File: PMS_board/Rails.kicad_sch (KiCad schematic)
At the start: 36 parts, among them J1 D1, J10 CORE, J11 DRIVE, J12 JETSON, J13 AUX1, J14 AUX2, J2 D2, J3 D3, J4 D4, J5 T1, J6 T2, J7 T3, J8 T4, J9 NET

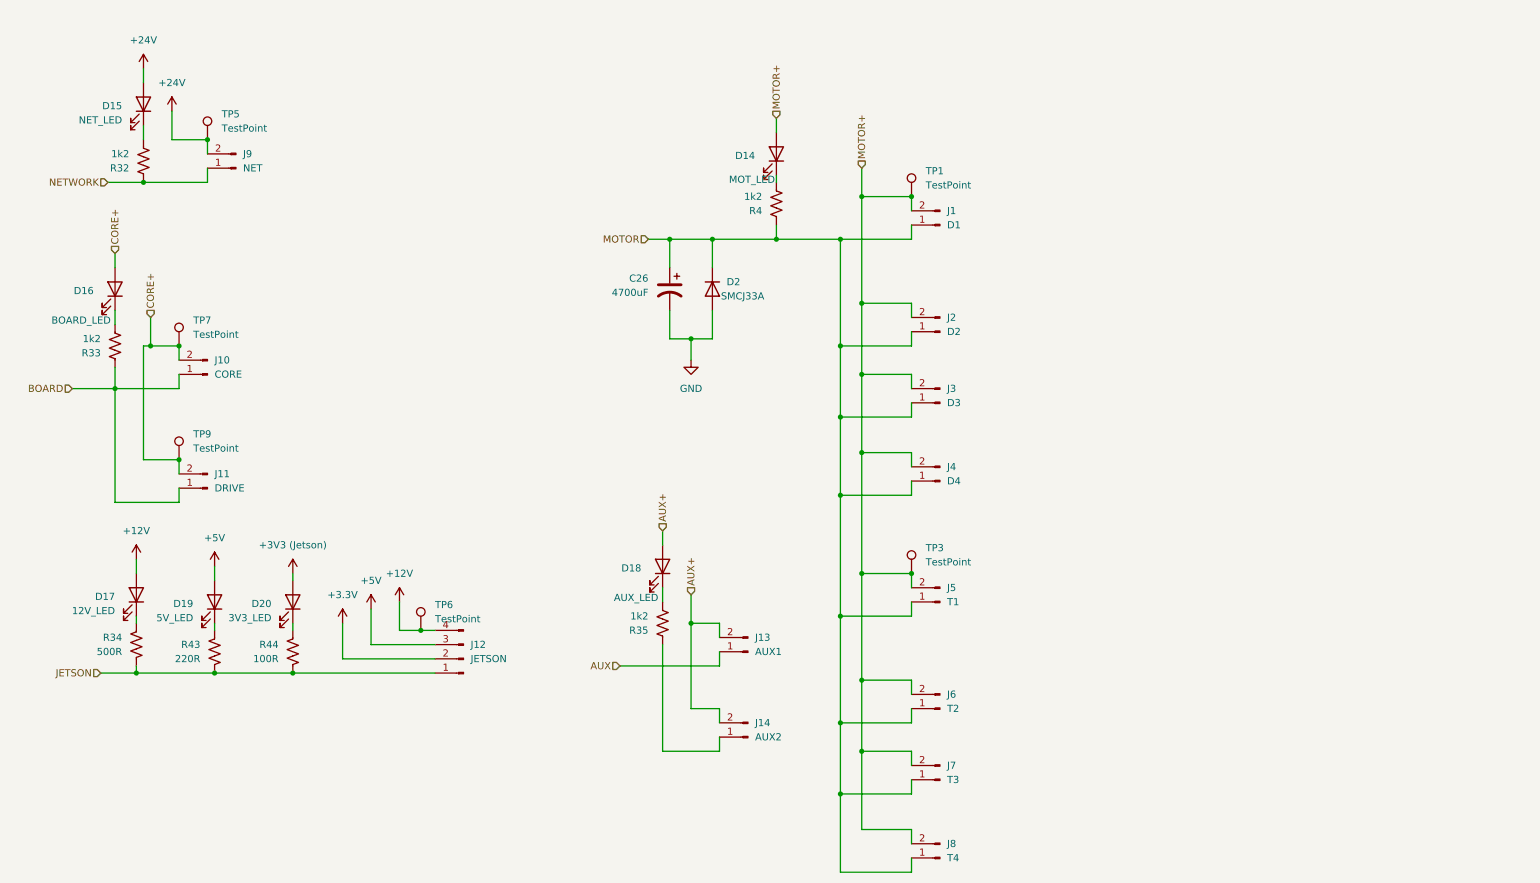
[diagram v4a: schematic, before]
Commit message: Added GND flags to Output rails and designated LEDs as green
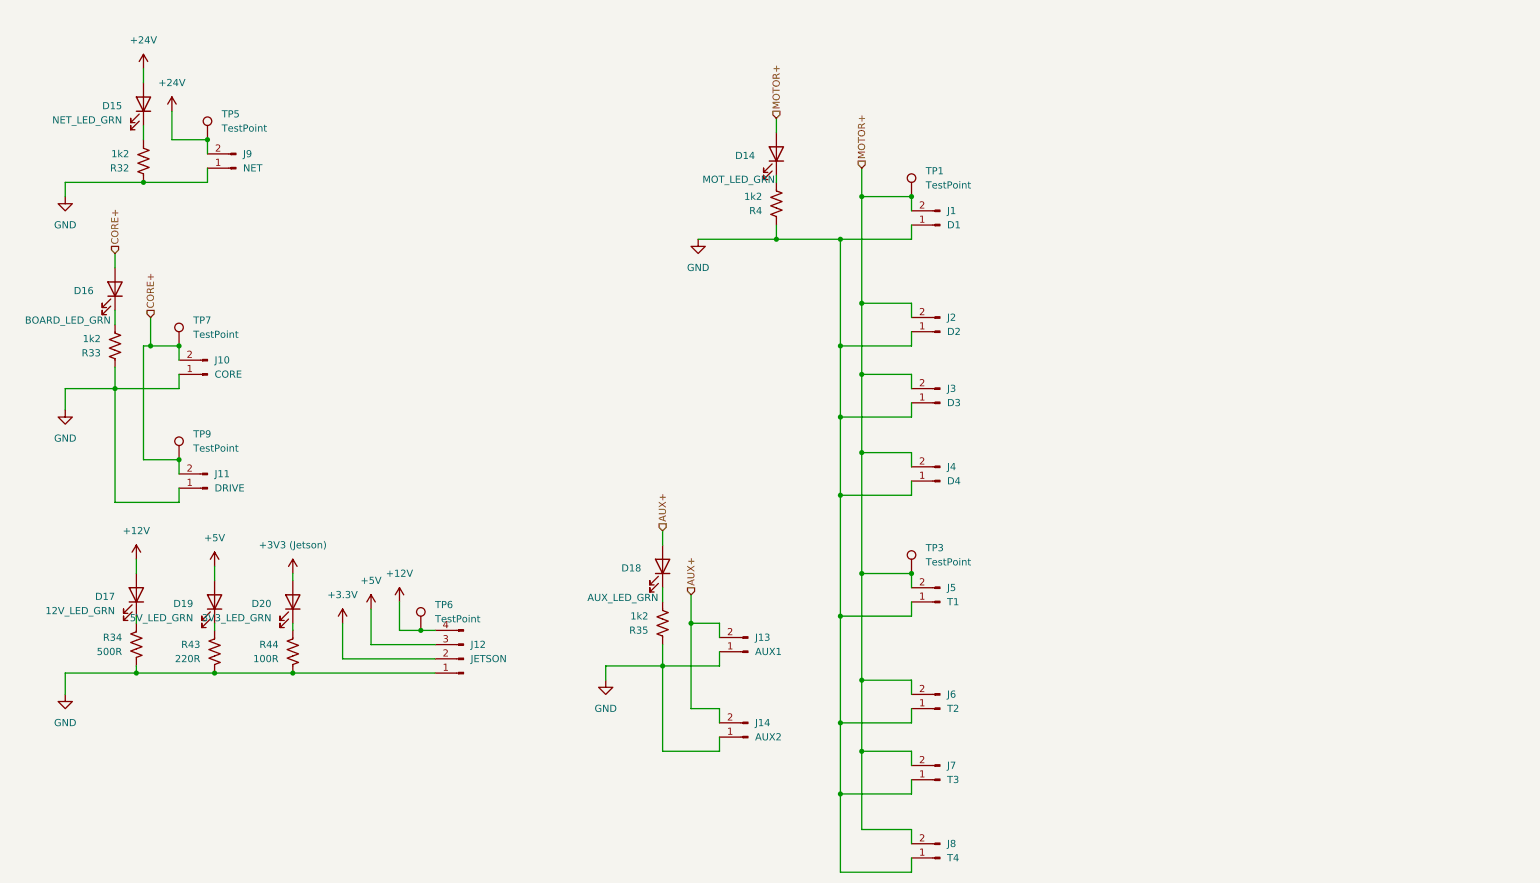
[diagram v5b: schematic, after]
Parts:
- removed C26: 4700uF, symbol Device:C_Polarized_US
- removed D2: SMCJ33A, symbol Device:D
- D14: value MOT_LED -> MOT_LED_GRN
- D15: value NET_LED -> NET_LED_GRN
- D16: value BOARD_LED -> BOARD_LED_GRN
- D17: value 12V_LED -> 12V_LED_GRN
- D18: value AUX_LED -> AUX_LED_GRN
- D19: value 5V_LED -> 5V_LED_GRN
- D20: value 3V3_LED -> 3V3_LED_GRN
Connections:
- net AUX is gone; now on net GND: J13.1 (Pin_1)
- net BOARD is gone; now on net GND: J10.1 (Pin_1), J11.1 (Pin_1), R33.1
- net JETSON is gone; now on net GND: J12.1 (Pin_1), R34.1, R43.1, R44.1
- net MOTOR is gone; now on net GND: J1.1 (Pin_1), J2.1 (Pin_1), J3.1 (Pin_1), J4.1 (Pin_1), J5.1 (Pin_1), J6.1 (Pin_1), J7.1 (Pin_1), J8.1 (Pin_1), R4.1
- net NETWORK is gone; now on net GND: J9.1 (Pin_1), R32.1
- net GND: now also J14.1 (Pin_1), R35.1

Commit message: Added another Jetson connector and hierachal pins for JET+ and NET+
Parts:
- added J15: JET2, symbol Connector:Conn_01x02_Pin
- J12: value JETSON -> JET1
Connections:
- net GND: now also J15.1 (Pin_1)
- net +12V renamed JET+
- net JET+: now also J15.2 (Pin_2)
- net +24V renamed NET+

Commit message: Finish Schematic
There's definitely stuff I missed, but I'm tired so we can review later. For my members to keep track of things, these are the changes/last minute additions I ran out of time to teach:
- brake chopper circuitry & reverse voltage protection for aux & motor rails
- microcontroller pinnouts
- net connections between sheets
- voltage resistors & system voltage measurements
- cell sense connectors & switch
- ADC routing
Please Please PLEASE ask questions about these additions. I don't want you guys to feel like you don't own this schematic, and I'm sorry I had to take away some of these designs to finish early. I definitely left too much on your plate to get everything perfect, which is my bad. I will happily walk through each and every circuit and help explain each part so you can better know your project when we get to reviewing and debugging later down the line.
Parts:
- removed D20: 3V3_LED_GRN, symbol Device:LED
- removed TP3, TP9: TestPoint, Relay_THT:Relay_DPDT_Schrack-RT2-FormC_RM5mm, symbol Connector:TestPoint
- added D23: 3V3_LED_GRN, symbol Device:LED
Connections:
- net +3V3 (Jetson): now also D23.2 (A)
- net at R44.2: now also D23.1 (K)
- net +3.3V renamed +3V3
